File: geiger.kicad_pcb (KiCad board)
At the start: 2 copper layers, 117.6 x 73.2 mm, 37 parts, among them SW1 SW_SPST, T1 IRFP450, T2 P55NF06, T3 BC517, U1 NE555P, U2 LM336Z25, U3 LM311, U4 STEP-DOWN-5V, U5 nodemcu-esp32, U6 GEIGERTUBE-STS6

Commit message: a
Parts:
- moved C2 2.69 mm to (57.9, 180.7), turned to 270 degrees
- moved C3 1.20 mm to (38.4, 148.0)
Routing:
- net GND: track 240.9 -> 35.1 mm
- net Net-(C2-Pad2): track 31.7 -> 27.8 mm
- net Net-(R32-Pad1): track 46.0 -> 42.3 mm
- net +8V: track 173.6 -> 176.1 mm
- net Net-(R31-Pad2): track 18.9 -> 21.0 mm
- net Net-(R4-Pad1): track 28.3 -> 27.3 mm
- net Net-(C3-Pad1): track 17.3 -> 16.3 mm
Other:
- board size 117.6 x 73.2 mm -> 117.5 x 73.2 mm
- net class AAA added: clearance 0.2, trace_width 1, via_dia 0.8, via_drill 0.4

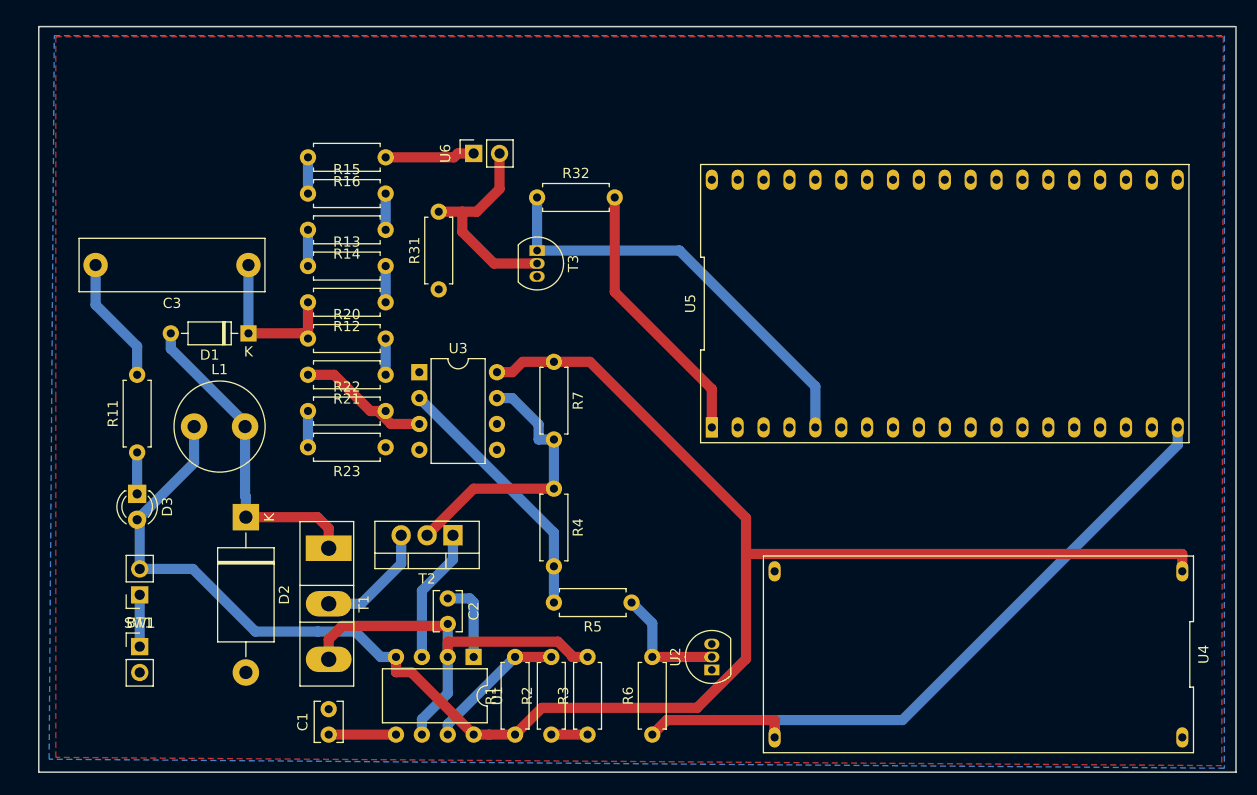
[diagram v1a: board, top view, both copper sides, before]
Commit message: Better connectors and minor trace improvements.
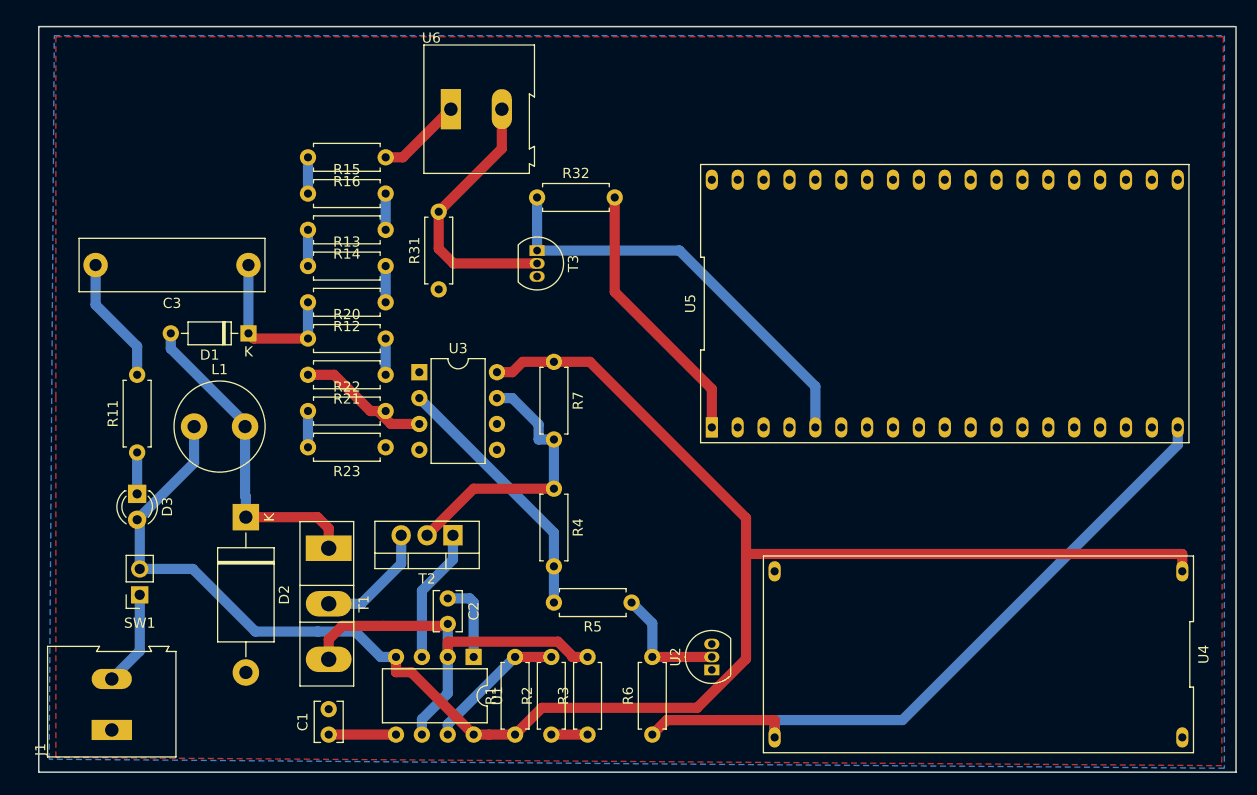
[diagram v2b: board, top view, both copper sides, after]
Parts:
- removed BT1: 2X18650 series, Connector_PinHeader_2.54mm:PinHeader_1x02_P2.54mm_Vertical
- added J1: Screw_Terminal_01x02, TerminalBlock:TerminalBlock_Altech_AK300-2_P5.00mm, F.Cu at (24.9, 193.6)
- U6: footprint Connector_PinSocket_2.54mm:PinSocket_1x02_P2.54mm_Vertical -> TerminalBlock:TerminalBlock_Altech_AK300-2_P5.00mm
- moved U6 4.88 mm to (58.2, 132.7), turned to 0 degrees
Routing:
- net Net-(R31-Pad2): track 21.0 -> 26.5 mm
- net Net-(J1-Pad2): track 5.08 -> 9.40 mm

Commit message: abc
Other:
- board size 117.5 x 73.2 mm -> 117 x 74 mm
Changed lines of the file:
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@@
     )
   )
-  (gr_line (start 17.78 124.587) (end 17.78 197.739) (layer Edge.Cuts) (width 0.15))
-  (gr_line (start 135.128 124.587) (end 17.78 124.587) (layer Edge.Cuts) (width 0.15))
-  (gr_line (start 135.255 197.739) (end 135.255 124.587) (layer Edge.Cuts) (width 0.15))
-  (gr_line (start 17.78 197.739) (end 135.255 197.739) (layer Edge.Cuts) (width 0.15))
+  (gr_line (start 16 124) (end 133 124) (layer Edge.Cuts) (width 0.05))
+  (gr_line (start 16 198) (end 16 124) (layer Edge.Cuts) (width 0.05))
+  (gr_line (start 133 198) (end 16 198) (layer Edge.Cuts) (width 0.05))
+  (gr_line (start 133 124) (end 133 198) (layer Edge.Cuts) (width 0.05))
   (segment (start 51.6431 183.388) (end 57.912 183.388) (width 1) (layer F.Cu) (net 1))
   (segment (start 46.228 184.7177) (end 47.5577 183.388) (width 1) (layer F.Cu) (net 1))
@@
     (polygon
       (pts
-        (xy 134.0104 125.5776) (xy 133.858 197.104) (xy 19.4564 196.2912) (xy 19.4564 160.9979) (xy 19.4564 125.5776)
+        (xy 132 197) (xy 17 197) (xy 17 125) (xy 132 125)
       )
     )
@@
     (polygon
       (pts
-        (xy 134.112 125.476) (xy 134.112 197.358) (xy 18.796 196.469) (xy 19.304 125.476)
+        (xy 132 197) (xy 17 197) (xy 17 125) (xy 132 125)
       )
     )
